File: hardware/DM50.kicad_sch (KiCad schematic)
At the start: 99 parts, among them J1 ST-LINK, J2 USB_C_Receptacle_USB2.0_14P, Q1 MMBT3904, SW10 CST, SW11 VAR, SW12 U, SW13 NXT, SW14 quote, SW15 STO, SW16 EVAL, SW17 L, SW18 D, SW19 R, SW2 F1, SW20 SIN, SW21 COS, SW22 TAN, SW23 SQR, SW24 y^x, SW25 1/x, SW26 ENTER, SW27 ENTER, SW28 +/-, SW29 EEX, SW3 F2, SW30 DEL, SW31 BACK, SW32 ALPHA, SW33 7, SW34 8, SW35 9, SW36 /, SW37 OPT1, SW38 4, SW39 5, SW4 F3, SW40 6, SW41 x, SW42 RESET, SW43 OPT2, SW44 1, SW45 2, SW46 3, SW47 -, SW48 ON, SW49 0, SW5 F4, SW50 ., SW51 SPC, SW52 +, SW6 F5, SW7 F6, SW8 MTH, SW9 PRG, U1 EA_DOGL128X-6, U2 STM32U535CBT6, U3 AT25SF641, U4 USBLC6-2SC6, U5 ADP2108AUJ-3.3, Y1 HSE 16MHz

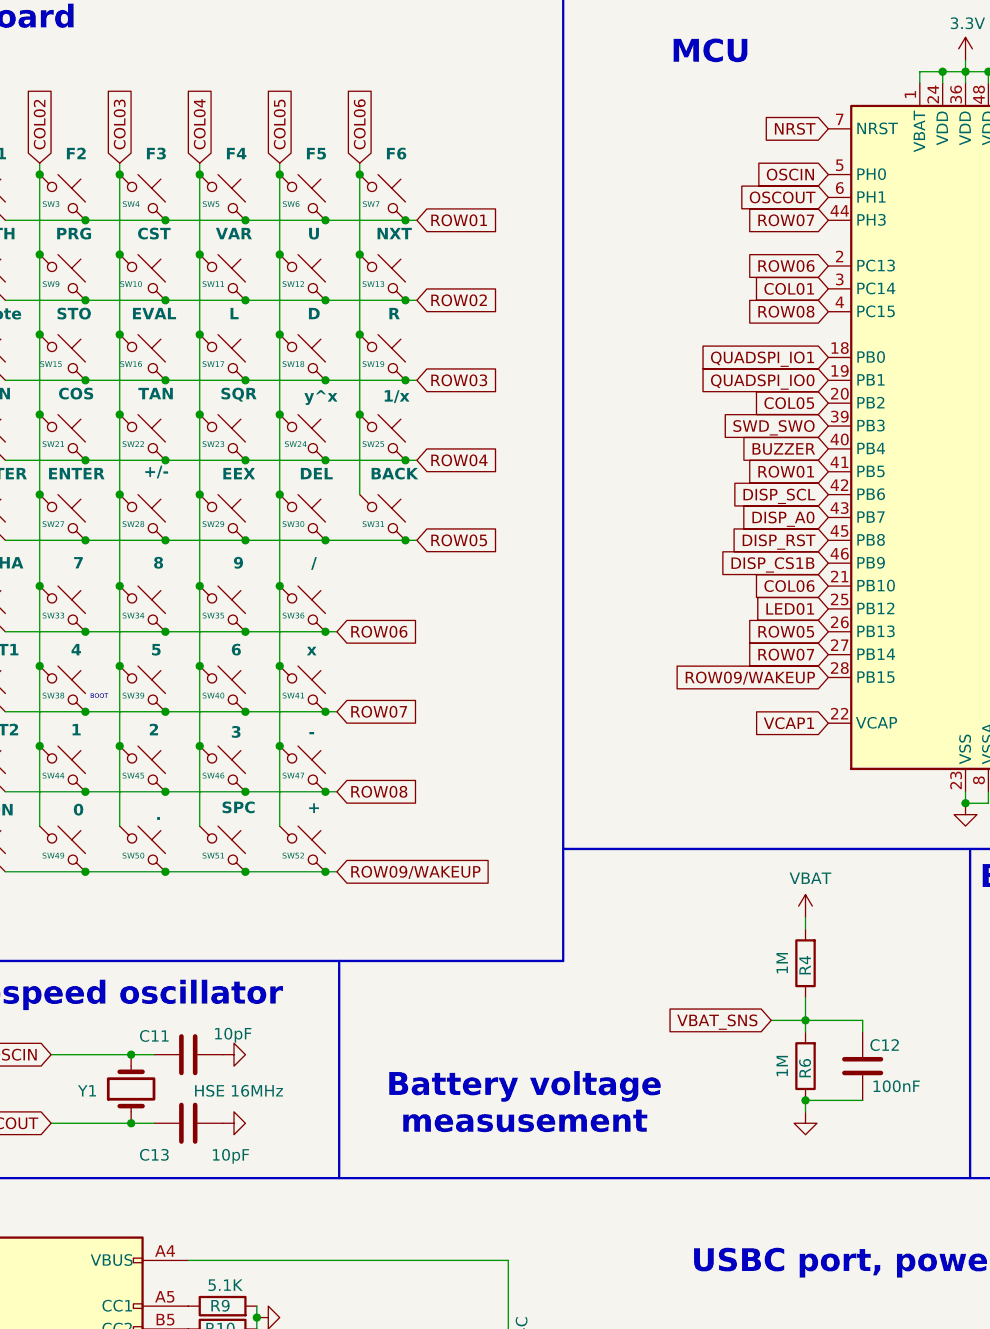
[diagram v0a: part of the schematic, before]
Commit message: crystal change
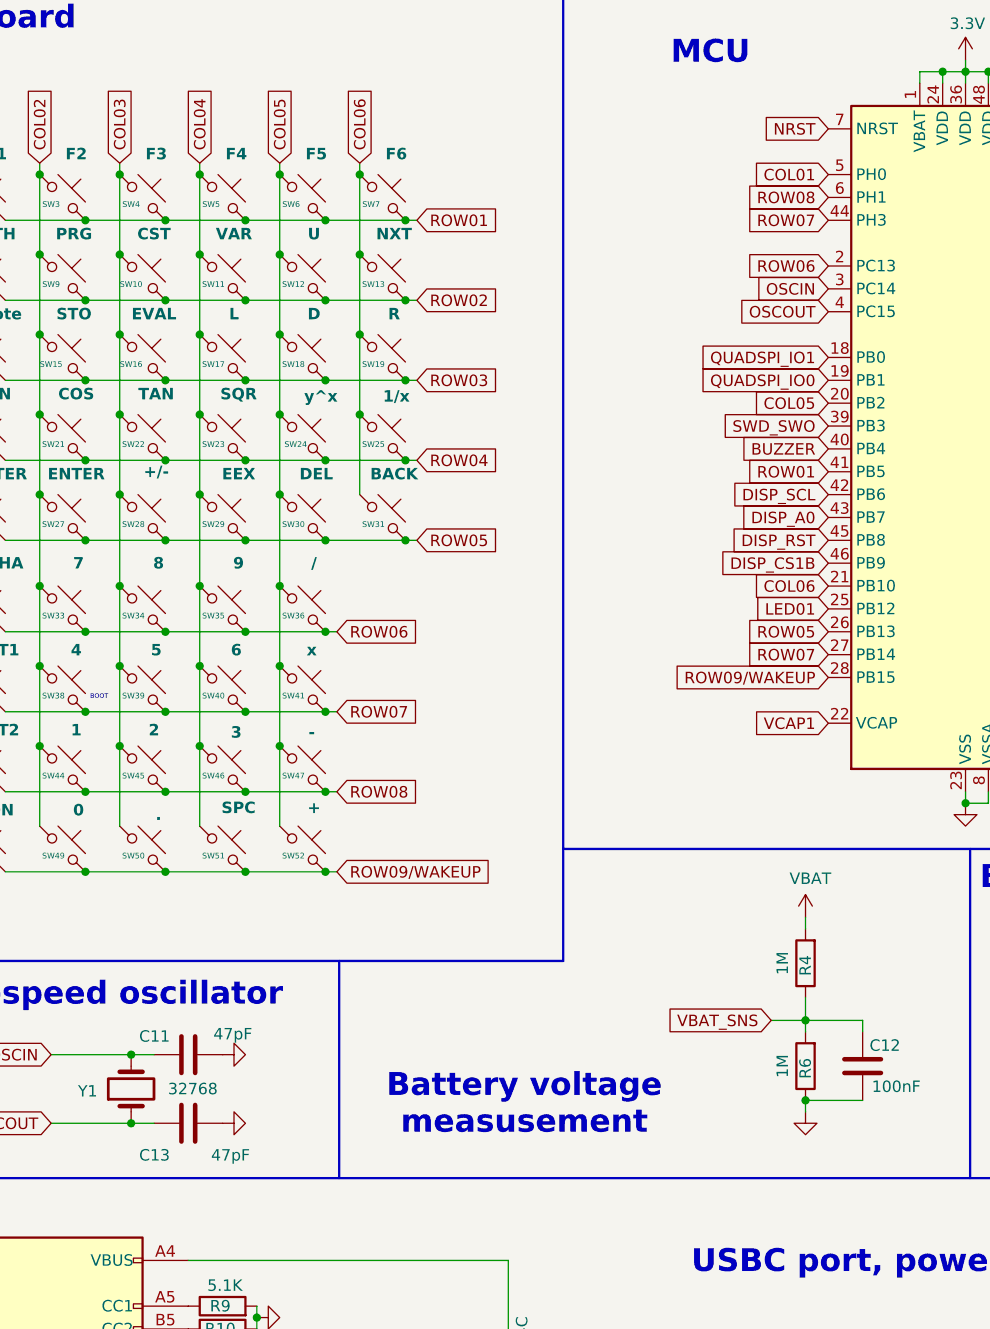
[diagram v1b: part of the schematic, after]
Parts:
- C11, C13: value 10pF -> 47pF
- Y1: value HSE 16MHz -> 32768; footprint Crystal:Crystal_SMD_0603-2Pin_6.0x3.5mm -> Crystal:Crystal_SMD_MicroCrystal_CM9V-T1A-2Pin_1.6x1.0mm
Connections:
- net COL01: now also U2.5 (PH0); no longer U2.3 (PC14)
- net OSCIN: now also U2.3 (PC14); no longer U2.5 (PH0)
- net OSCOUT: now also U2.4 (PC15); no longer U2.6 (PH1)
- net ROW08: now also U2.6 (PH1); no longer U2.4 (PC15)
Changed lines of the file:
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@@
 	(global_label "COL01"
 		(shape input)
-		(at 118.11 45.72 180)
+		(at 118.11 33.02 180)
 		(fields_autoplaced yes)
 		(effects
@@
 		)
 		(property "Intersheetrefs" "${INTERSHEET_REFS}"
-			(at 109.0772 45.72 0)
+			(at 109.0772 33.02 0)
 			(effects
 				(font
@@
 	(global_label "OSCOUT"
 		(shape input)
-		(at 118.11 35.56 180)
+		(at 118.11 48.26 180)
 		(fields_autoplaced yes)
 		(effects
@@
 		)
 		(property "Intersheetrefs" "${INTERSHEET_REFS}"
-			(at 107.6862 35.56 0)
+			(at 107.6862 48.26 0)
 			(effects
 				(font
@@
 	(global_label "OSCIN"
 		(shape input)
-		(at 118.11 33.02 180)
+		(at 118.11 45.72 180)
 		(fields_autoplaced yes)
 		(effects
@@
 		)
 		(property "Intersheetrefs" "${INTERSHEET_REFS}"
-			(at 109.3795 33.02 0)
+			(at 109.3795 45.72 0)
 			(effects
 				(font
@@
 	(global_label "ROW08"
 		(shape input)
-		(at 118.11 48.26 180)
+		(at 118.11 35.56 180)
 		(fields_autoplaced yes)
 		(effects
@@
 		)
 		(property "Intersheetrefs" "${INTERSHEET_REFS}"
-			(at 108.6539 48.26 0)
+			(at 108.6539 35.56 0)
 			(effects
 				(font
@@
 			)
 		)
-		(property "Value" "10pF"
+		(property "Value" "47pF"
 			(at 53.848 141.986 90)
 			(effects
@@
 			)
 		)
-		(property "Value" "HSE 16MHz"
-			(at 52.578 134.874 90)
+		(property "Value" "32768"
+			(at 47.498 134.62 90)
 			(effects
 				(font
@@
 			)
 		)
-		(property "Footprint" "Crystal:Crystal_SMD_0603-2Pin_6.0x3.5mm"
+		(property "Footprint" "Crystal:Crystal_SMD_MicroCrystal_CM9V-T1A-2Pin_1.6x1.0mm"
 			(at 40.64 134.62 0)
 			(effects
@@
 			)
 		)
-		(property "Value" "10pF"
+		(property "Value" "47pF"
 			(at 54.102 128.524 90)
 			(effects

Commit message: pcb changes
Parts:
- removed R12: 10K, Resistor_SMD:R_0603_1608Metric, symbol Device:R
- added SW1: PGM, Button_Switch_SMD:SW_SPST_TL3342, symbol Switch:SW_Push
- R1: value 100k -> 10k
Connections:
- net 3.3V: now also SW1.1
- net BOOT0: now also SW1.2; no longer SW37.2, SW38.2, SW39.2, SW40.2, SW41.2, U2.27 (PB14)
- new net ROW07: SW37.2, SW38.2, SW39.2, SW40.2, SW41.2, U2.27 (PB14)
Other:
- note added: "RESET & PGM"
- note removed: "BOOT0 = 0 = Flash BOOT1 = 1 = DFU"
- note removed: "Boot mode"
- note removed: "KEY COL02 - ROW07"
- moved on the sheet: C10, R1, R2, SW42

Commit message: pcb changes
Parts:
- C11, C13: value 47pF -> 9pF
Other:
- note added: "Debug port"
- note removed: "Reset and debug port"
- moved on the sheet: J1
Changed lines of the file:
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@@
 		)
 	)
-	(text "Reset and debug port"
+	(text "Debug port"
 		(exclude_from_sim no)
-		(at 178.308 69.85 0)
+		(at 182.372 17.78 0)
 		(effects
 			(font
@@
 	(global_label "SWD_SWDIO"
 		(shape input)
-		(at 189.23 92.71 0)
+		(at 191.77 43.18 0)
 		(fields_autoplaced yes)
 		(effects
@@
 		)
 		(property "Intersheetrefs" "${INTERSHEET_REFS}"
-			(at 202.9799 92.71 0)
+			(at 205.5199 43.18 0)
 			(effects
 				(font
@@
 	(global_label "NRST"
 		(shape input)
-		(at 189.23 87.63 0)
+		(at 191.77 38.1 0)
 		(fields_autoplaced yes)
 		(effects
@@
 		)
 		(property "Intersheetrefs" "${INTERSHEET_REFS}"
-			(at 196.9928 87.63 0)
+			(at 199.5328 38.1 0)
 			(effects
 				(font
@@
 	(global_label "SWD_SWCLK"
 		(shape input)
-		(at 189.23 90.17 0)
+		(at 191.77 40.64 0)
 		(fields_autoplaced yes)
 		(effects
@@
 		)
 		(property "Intersheetrefs" "${INTERSHEET_REFS}"
-			(at 203.3427 90.17 0)
+			(at 205.8827 40.64 0)
 			(effects
 				(font
@@
 	(global_label "SWD_SWO"
 		(shape input)
-		(at 189.23 85.09 0)
+		(at 191.77 35.56 0)
 		(fields_autoplaced yes)
 		(effects
@@
 		)
 		(property "Intersheetrefs" "${INTERSHEET_REFS}"
-			(at 201.1051 85.09 0)
+			(at 203.6451 35.56 0)
 			(effects
 				(font
@@
 			)
 		)
-		(property "Datasheet" "~"
+		(property "Datasheet" "https://www.digikey.es/en/products/detail/yageo/CC0603KRX7R7BB105/2833611"
 			(at 220.98 44.45 0)
 			(effects
@@
 			)
 		)
-		(property "Datasheet" "~"
+		(property "Datasheet" "https://www.digikey.es/en/products/detail/yageo/CC0603KRX7R7BB105/2833611"
 			(at 275.59 44.45 0)
 			(effects
@@
 			)
 		)
-		(property "Datasheet" "~"
+		(property "Datasheet" "https://www.digikey.es/en/products/detail/soberton-inc/PT-1403-3/9924397"
 			(at 269.875 142.24 90)
 			(effects
@@
 			)
 		)
-		(property "Datasheet" "~"
+		(property "Datasheet" "https://www.digikey.es/en/products/detail/yageo/CC0603KRX7R7BB105/2833611"
 			(at 266.7 36.83 0)
 			(effects
@@
 			)
 		)
-		(property "Datasheet" "~"
+		(property "Datasheet" "https://www.digikey.es/en/products/detail/c-k/PTS526-SK15-SMTR2-LFS/10056626"
 			(at 152.4 133.35 0)
 			(effects
@@
 			)
 		)
-		(property "Datasheet" "~"
+		(property "Datasheet" "https://www.digikey.es/en/products/detail/yageo/CC0603KRX7R7BB105/2833611"
 			(at 266.7 46.99 0)
 			(effects
@@
 			)
 		)
-		(property "Datasheet" "~"
+		(property "Datasheet" "https://www.digikey.es/en/products/detail/yageo/CC0603KRX7R7BB105/2833611"
 			(at 220.98 54.61 0)
 			(effects
@@
 	(symbol
 		(lib_id "power:GND")
-		(at 189.23 95.25 0)
+		(at 191.77 45.72 0)
 		(unit 1)
 		(exclude_from_sim no)
@@
 		(fields_autoplaced yes)
 		(property "Reference" "#PWR010"
-			(at 189.23 101.6 0)
+			(at 191.77 52.07 0)
 			(effects
 				(font
@@
 		)
 		(property "Value" "GND"
-			(at 189.23 100.33 0)
+			(at 191.77 50.8 0)
 			(effects
 				(font
@@
 		)
 		(property "Footprint" ""
-			(at 189.23 95.25 0)
+			(at 191.77 45.72 0)
 			(effects
 				(font
@@
 		)
 		(property "Datasheet" ""
-			(at 189.23 95.25 0)
+			(at 191.77 45.72 0)
 			(effects
 				(font
@@
 		)
 		(property "Description" ""
-			(at 189.23 95.25 0)
+			(at 191.77 45.72 0)
 			(effects
 				(font
@@
 			)
 		)
-		(property "Datasheet" "~"
+		(property "Datasheet" "https://www.digikey.es/en/products/detail/yageo/CC0603KRX7R7BB105/2833611"
 			(at 266.7 52.07 0)
 			(effects
@@
 			)
 		)
-		(property "Value" "47pF"
-			(at 53.848 141.986 90)
+		(property "Value" "9pF"
+			(at 52.324 141.986 90)
 			(effects
 				(font
@@
 			)
 		)
-		(property "Datasheet" "~"
+		(property "Datasheet" "https://www.digikey.es/en/products/detail/yageo/CC0603KRX7R7BB105/2833611"
 			(at 275.59 39.37 0)
 			(effects
@@
 			)
 		)
-		(property "Datasheet" "~"
+		(property "Datasheet" "https://www.digikey.es/en/products/detail/c-k/PTS526-SK15-SMTR2-LFS/10056626"
 			(at 170.18 125.73 0)
 			(effects
@@
 			)
 		)
-		(property "Value" "47pF"
-			(at 54.102 128.524 90)
+		(property "Value" "9pF"
+			(at 52.324 128.778 90)
 			(effects
 				(font
@@
 			)
 		)
-		(property "Datasheet" "~"
+		(property "Datasheet" "https://www.digikey.es/en/products/detail/yageo/CC0603KRX7R7BB105/2833611"
 			(at 266.7 41.91 0)
 			(effects
@@
 	(symbol
 		(lib_id "Connector_Generic:Conn_01x05")
-		(at 184.15 90.17 180)
+		(at 186.69 40.64 180)
 		(unit 1)
 		(exclude_from_sim no)
@@
 		(dnp no)
 		(property "Reference" "J1"
-			(at 183.896 82.55 0)
+			(at 186.436 33.02 0)
 			(effects
 				(font
@@
 		)
 		(property "Value" "ST-LINK"
-			(at 181.61 90.17 90)
+			(at 184.15 40.64 90)
 			(effects
 				(font
@@
 		)
 		(property "Footprint" "DM50:JST_CON_SMD"
-			(at 184.15 90.17 0)
+			(at 186.69 40.64 0)
 			(effects
 				(font
@@
 		)
 		(property "Datasheet" "~"
-			(at 184.15 90.17 0)
+			(at 186.69 40.64 0)
 			(effects
 				(font
@@
 		)
 		(property "Description" "Generic connector, single row, 01x05, script generated (kicad-library-utils/schlib/autogen/connector/)"
-			(at 184.15 90.17 0)
+			(at 186.69 40.64 0)
 			(effects
 				(font
@@
 			)
 		)
-		(property "Datasheet" "~"
+		(property "Datasheet" "https://www.digikey.es/en/products/detail/yageo/CC0603KRX7R7BB105/2833611"
 			(at 220.98 49.53 0)
 			(effects

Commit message: Update DM50.kicad_sch
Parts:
- R1, R2: value 10k -> 10K
- SW1: value PGM -> SW_SPST
- SW10: value CST -> BT_SMD
- SW11: value VAR -> BT_SMD
- SW12: value U -> BT_SMD
- SW13: value NXT -> BT_SMD
- SW14: value quote -> BT_SMD
- SW15: value STO -> BT_SMD
- SW16: value EVAL -> BT_SMD
- SW17: value L -> BT_SMD
- SW18: value D -> BT_SMD
- SW19: value R -> BT_SMD
- SW2: value F1 -> BT_SMD
- SW20: value SIN -> BT_SMD
- SW21: value COS -> BT_SMD
- SW22: value TAN -> BT_SMD
- SW23: value SQR -> BT_SMD
- SW24: value y^x -> BT_SMD
- SW25: value 1/x -> BT_SMD
- SW26, SW27: value ENTER -> BT_SMD
- SW28: value +/- -> BT_SMD
- SW29: value EEX -> BT_SMD
- SW3: value F2 -> BT_SMD
- SW30: value DEL -> BT_SMD
- SW31: value BACK -> BT_SMD
- SW32: value ALPHA -> BT_SMD
- SW33: value 7 -> BT_SMD
- SW34: value 8 -> BT_SMD
- SW35: value 9 -> BT_SMD
- SW36: value / -> BT_SMD
- SW37: value OPT1 -> BT_SMD
- SW38: value 4 -> BT_SMD
- SW39: value 5 -> BT_SMD
- SW4: value F3 -> BT_SMD
- SW40: value 6 -> BT_SMD
- SW41: value x -> BT_SMD
- SW42: value RESET -> SW_SPST
- SW43: value OPT2 -> BT_SMD
- SW44: value 1 -> BT_SMD
- SW45: value 2 -> BT_SMD
- SW46: value 3 -> BT_SMD
- SW47: value - -> BT_SMD
- SW48: value ON -> BT_SMD
- SW49: value 0 -> BT_SMD
- SW5: value F4 -> BT_SMD
- SW50: value . -> BT_SMD
- SW51: value SPC -> BT_SMD
- SW52: value + -> BT_SMD
- SW6: value F5 -> BT_SMD
- SW7: value F6 -> BT_SMD
- SW8: value MTH -> BT_SMD
- SW9: value PRG -> BT_SMD

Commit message: pcb changes
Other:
- note added: "GPIO_PULLUP"
- note removed: "Power button"
- moved on the sheet: D1, R1, R3, R5, SW1, SW10, SW11, SW12, SW13, SW14, SW15, SW16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

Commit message: 3d changes (step files)
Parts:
- added C22, C23: 4.7 uF, Capacitor_SMD:C_0603_1608Metric, symbol Device:C
- added D3: LED (RED), LED_SMD:LED_0603_1608Metric, symbol Device:LED
- added J3: S2B-PH-K-SLFSN, DM50:CONN_S2B-PH-K-S_JST, symbol DM50:S2B-PH-K-SLFSN
- added R12: 2K, Resistor_SMD:R_0603_1608Metric, symbol Device:R
- added R13: 1.5K, Resistor_SMD:R_0603_1608Metric, symbol Device:R
- added U6: MCP73831-2-OT, Package_TO_SOT_SMD:SOT-23-5, symbol Battery_Management:MCP73831-2-OT
- D1: value LED (RED) -> LED (GREEN)
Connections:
- net GND: now also C22.1, C23.2, J3.2, R12.1, U6.2 (V_{SS})
- net VBAT: now also C23.1, J3.1, U6.3 (V_{BAT})
- net VBUS: now reaches D2.2, J2.A4 (VBUS), J2.A9 (VBUS), J2.B4 (VBUS), J2.B9 (VBUS), U4.5 (VBUS)
- net VBUS: now also C22.2, R13.2, U6.4 (V_{DD})
- new net: R12.2, U6.5 (PROG)
- new net: D3.1 (K), U6.1 (STAT)
- new net: D3.2 (A), R13.1
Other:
- note added: "(optional)"
- note added: "LiPO"
- note added: "LiPO OR 2xAA"
- note added: "Oscillator"
- note removed: "High-speed oscillator"

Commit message: pcb changes
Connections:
- net 3.3V: no longer U2.1 (VBAT)
- net VBAT: now also U2.1 (VBAT); no longer R4.2
- net VINPUT: now reaches C20.1, D2.3, R11.1, U5.1 (Vin)
- net VINPUT: now also R4.2

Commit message: pcb changes
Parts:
- removed J3: S2B-PH-K-SLFSN, DM50:CONN_S2B-PH-K-S_JST, symbol DM50:S2B-PH-K-SLFSN
- added J4: Conn_01x04, DM50:CONN_S2B-ZR-SM4A-TFLFSN_JST, symbol Connector_Generic:Conn_01x04
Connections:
- net GND: now also J4.2 (Pin_2), J4.3 (Pin_3), J4.4 (Pin_4)
- net VBAT: now also J4.1 (Pin_1)
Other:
- moved on the sheet: C22, C23, D3, R12, R13, U6
